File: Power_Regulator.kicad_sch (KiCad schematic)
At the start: 2 parts

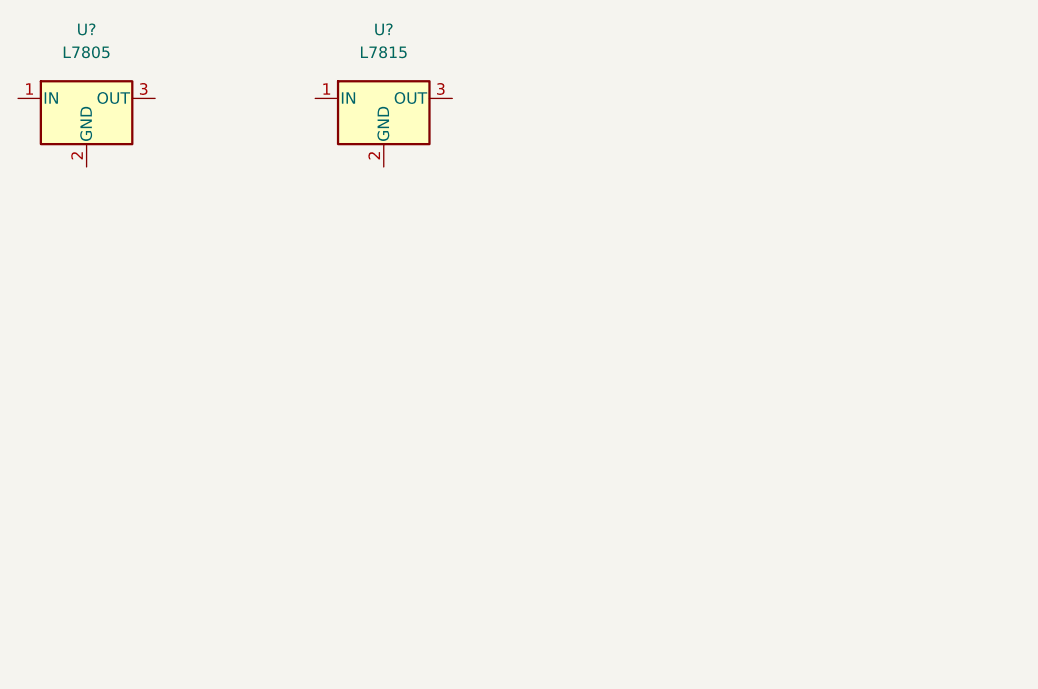
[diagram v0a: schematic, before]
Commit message: Finished basic schematic.
Need to add inline opamps and footprints to all components.
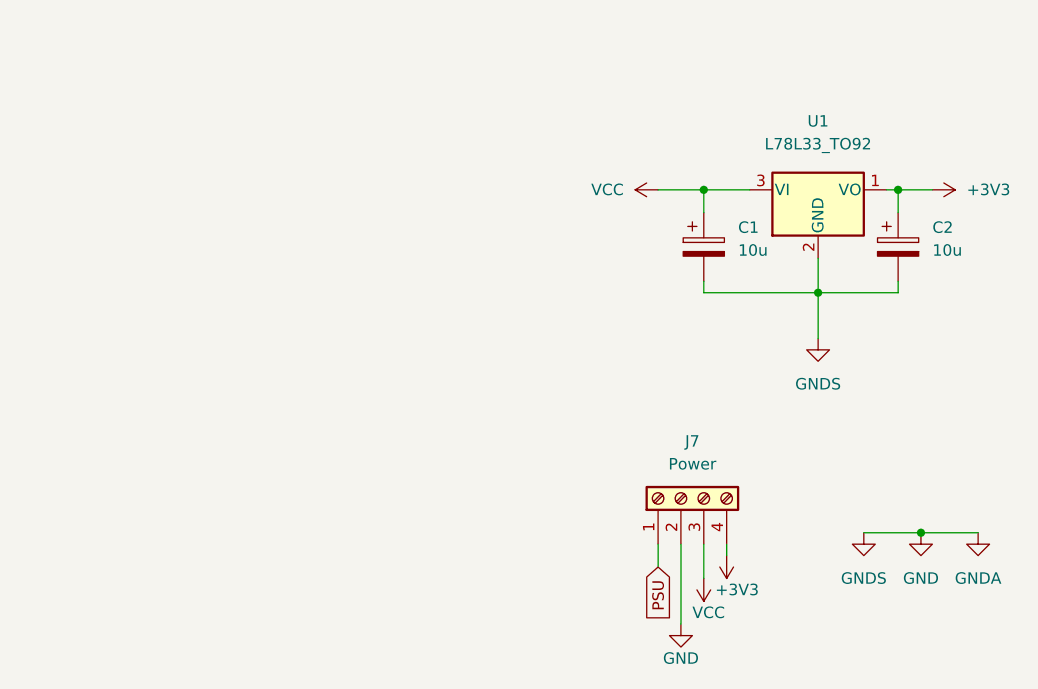
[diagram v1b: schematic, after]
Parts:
- removed U?: L7805, Package_TO_SOT_THT:TO-220-3_Horizontal_TabDown, symbol Regulator_Linear:L7805
- removed U?: L7815, Package_TO_SOT_THT:TO-220-3_Horizontal_TabDown, symbol Regulator_Linear:L7815
- added C1, C2: 10u, symbol Device:C_Polarized
- added J7: Power, symbol Connector:Screw_Terminal_01x04
- added U1: L78L33_TO92, Package_TO_SOT_THT:TO-92_Inline, symbol Regulator_Linear:L78L33_TO92
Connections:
- new net +3V3: C2.1, J7.4 (Pin_4), U1.1 (VO)
- new net GND: C1.2, C2.2, J7.2 (Pin_2), U1.2 (GND)
- new net PSU: J7.1 (Pin_1)
- new net VCC: C1.1, J7.3 (Pin_3), U1.3 (VI)
